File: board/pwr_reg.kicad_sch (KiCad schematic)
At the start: 52 parts, among them J2 9V-30VDC, Q1 IRF9540N, Q2 2N3906, Q3 IRF9540N, Q4 2N3906, SW1 On/Off, SW2 RESET, U1 LM350, U2 LM350, U3 LM350

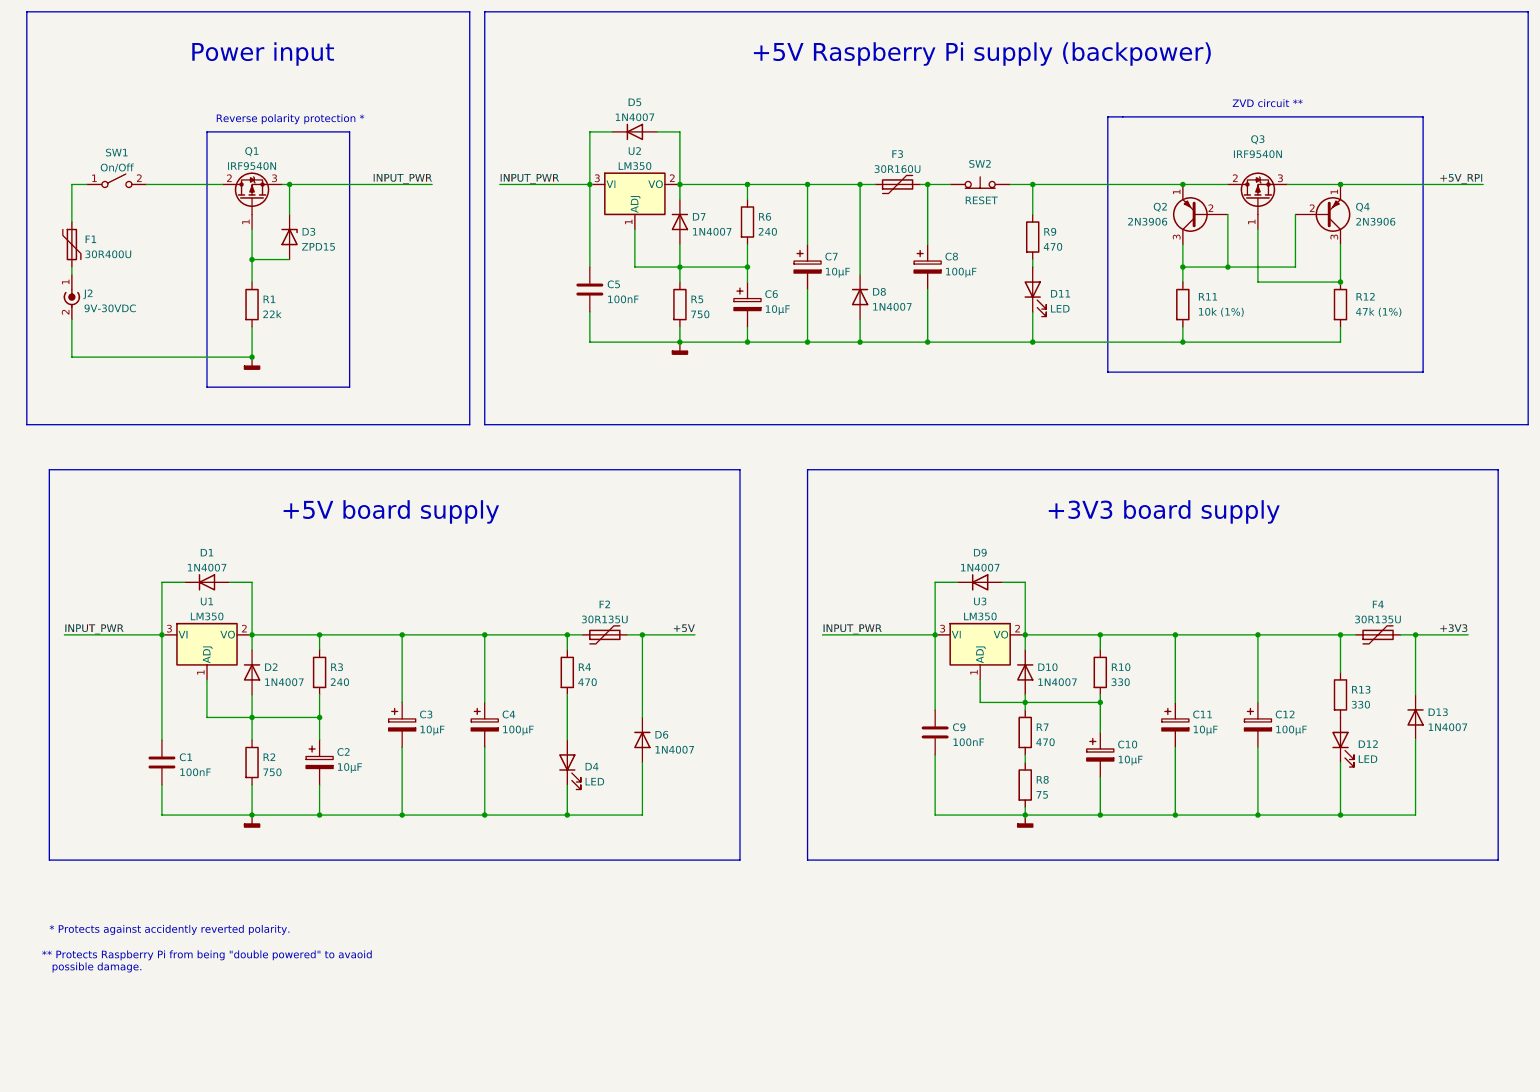
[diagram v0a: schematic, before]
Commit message: Make it a multiboard project.
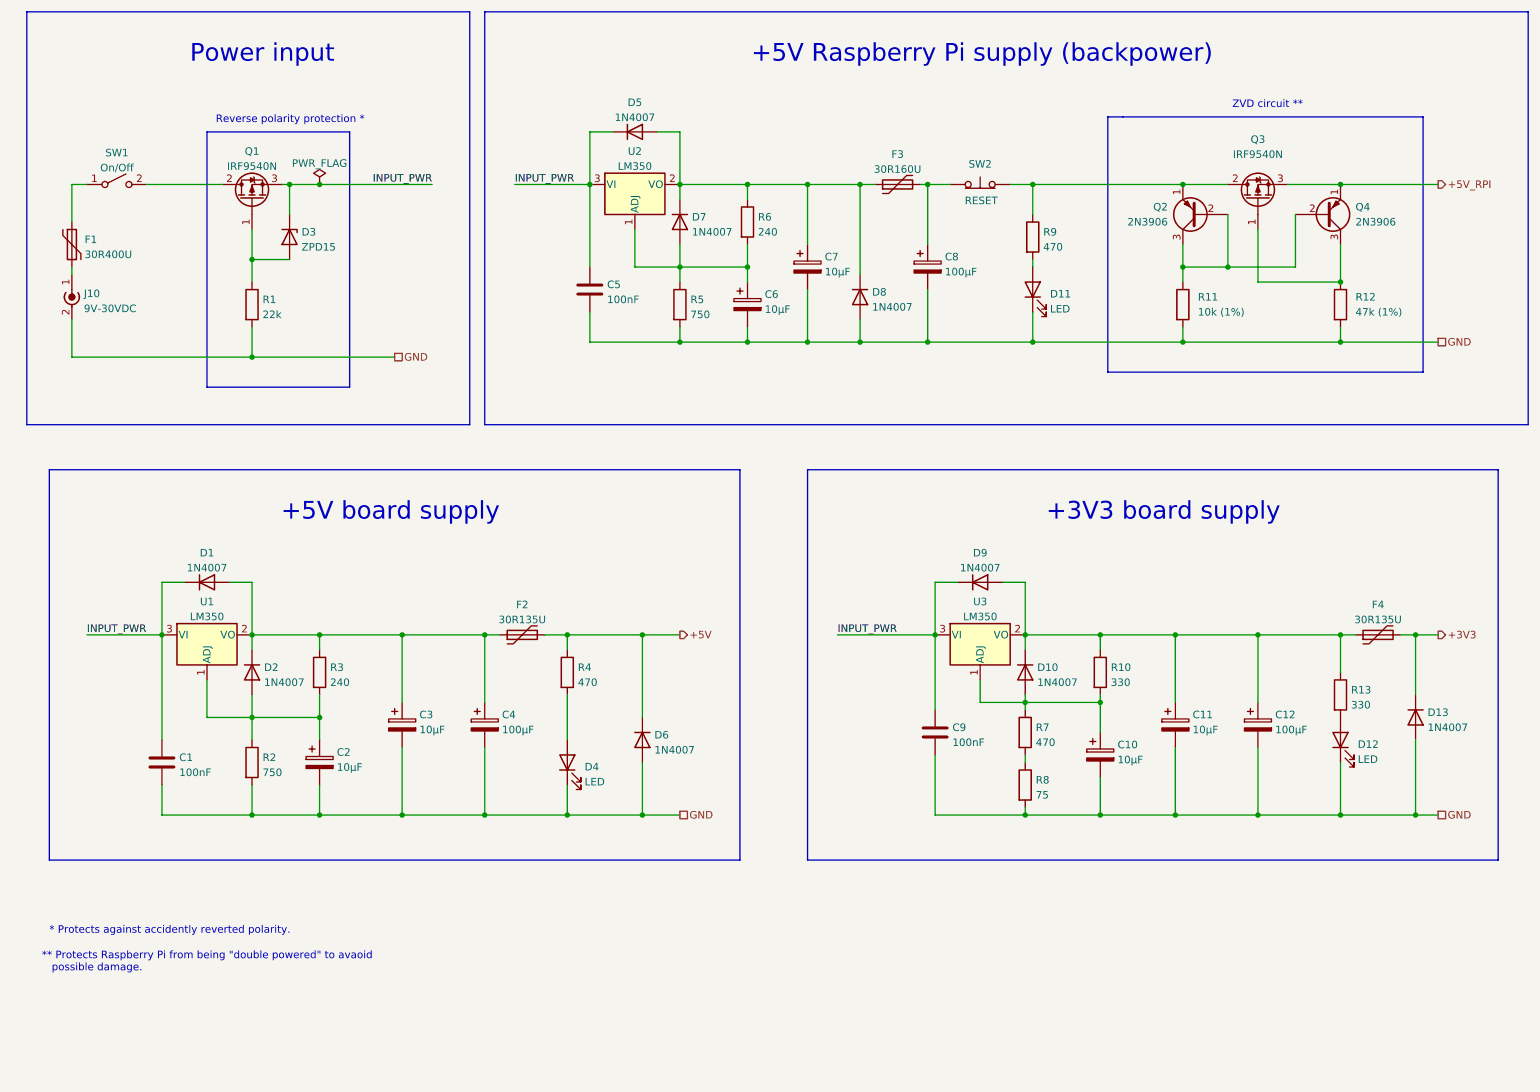
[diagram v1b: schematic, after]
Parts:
- renumbered J2 to J10
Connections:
- net +5V: now also R4.1
- net at C3.1, C4.1, D1.2 (A)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: no longer R4.1
- net GNDD renamed GND
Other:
- moved on the sheet: F2

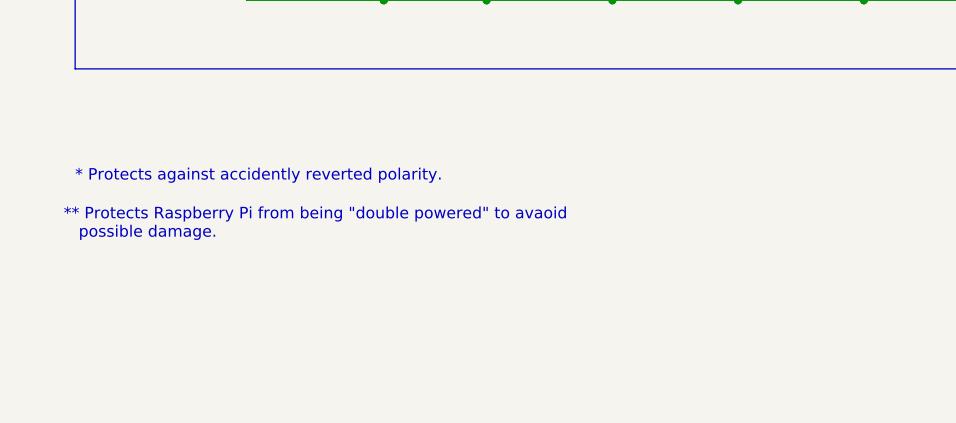
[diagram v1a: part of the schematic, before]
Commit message: Modularize board.
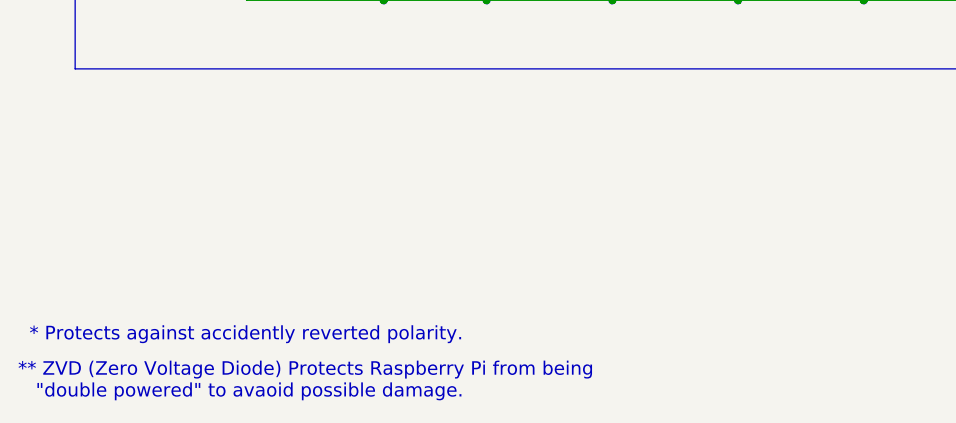
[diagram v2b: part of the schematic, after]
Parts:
- D1, D10, D13, D2, D5, D6, D7, D8, D9: footprint Diode_THT:D_DO-41_SOD81_P10.16mm_Horizontal -> Diode_THT:D_DO-41_SOD81_P5.08mm_Vertical_KathodeUp
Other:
- note added: "** ZVD (Zero Voltage Diode) Protects Raspberry Pi from being "double powered" to avaoid possible damage."
- note removed: "** Protects Raspberry Pi from being "double powered" to avaoid possible damage."
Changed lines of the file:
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@@
   (title_block
     (title "The Ulysses Board")
-    (date "2022-09-08")
+    (date "2022-09-15")
     (rev "1.3")
     (company "Dirk Gottschalk")
@@
     (effects (font (size 1.27 1.27)) (justify right bottom))
   )
-  (text "* Protects against accidently reverted polarity." (at 21.59 171.45 0)
-    (effects (font (size 1.27 1.27)) (justify left bottom))
+  (text "* Protects against accidently reverted polarity." (at 16.51 189.23 0)
+    (effects (font (size 1.5 1.5)) (justify left bottom))
   )
   (text "Reverse polarity protection *" (at 74.93 34.29 180)
@@
     (effects (font (size 3 3)) (justify right bottom))
   )
-  (text "** Protects Raspberry Pi from being \"double powered\" to avaoid\n   possible damage."
-    (at 20.32 177.8 0)
-    (effects (font (size 1.27 1.27)) (justify left bottom))
+  (text "** ZVD (Zero Voltage Diode) Protects Raspberry Pi from being\n   \"double powered\" to avaoid possible damage."
+    (at 15.24 195.58 0)
+    (effects (font (size 1.5 1.5)) (justify left bottom))
   )
   (text "+3V3 board supply" (at 229.87 101.6 180)
@@
     (property "Reference" "D9" (id 0) (at 179.07 106.7902 0))
     (property "Value" "1N4007" (id 1) (at 179.07 109.3271 0))
-    (property "Footprint" "Diode_THT:D_DO-41_SOD81_P10.16mm_Horizontal" (id 2) (at 179.07 116.205 0)
+    (property "Footprint" "Diode_THT:D_DO-41_SOD81_P5.08mm_Vertical_KathodeUp" (id 2) (at 179.07 116.205 0)
       (effects (font (size 1.27 1.27)) hide)
     )
@@
     (property "Reference" "D5" (id 0) (at 120.65 30.5902 0))
     (property "Value" "1N4007" (id 1) (at 120.65 33.1271 0))
-    (property "Footprint" "Diode_THT:D_DO-41_SOD81_P10.16mm_Horizontal" (id 2) (at 120.65 40.005 0)
+    (property "Footprint" "Diode_THT:D_DO-41_SOD81_P5.08mm_Vertical_KathodeUp" (id 2) (at 120.65 40.005 0)
       (effects (font (size 1.27 1.27)) hide)
     )
@@
       (effects (font (size 1.27 1.27)) (justify left))
     )
-    (property "Footprint" "Diode_THT:D_DO-41_SOD81_P10.16mm_Horizontal" (id 2) (at 182.245 127 0)
+    (property "Footprint" "Diode_THT:D_DO-41_SOD81_P5.08mm_Vertical_KathodeUp" (id 2) (at 182.245 127 0)
       (effects (font (size 1.27 1.27)) hide)
     )
@@
       (effects (font (size 1.27 1.27)) (justify left))
     )
-    (property "Footprint" "Diode_THT:D_DO-41_SOD81_P10.16mm_Horizontal" (id 2) (at 154.305 63.5 0)
+    (property "Footprint" "Diode_THT:D_DO-41_SOD81_P5.08mm_Vertical_KathodeUp" (id 2) (at 154.305 63.5 0)
       (effects (font (size 1.27 1.27)) hide)
     )
@@
       (effects (font (size 1.27 1.27)) (justify left))
     )
-    (property "Footprint" "Diode_THT:D_DO-41_SOD81_P10.16mm_Horizontal" (id 2) (at 123.825 50.8 0)
+    (property "Footprint" "Diode_THT:D_DO-41_SOD81_P5.08mm_Vertical_KathodeUp" (id 2) (at 123.825 50.8 0)
       (effects (font (size 1.27 1.27)) hide)
     )
@@
     (property "Reference" "D1" (id 0) (at 48.26 106.7902 0))
     (property "Value" "1N4007" (id 1) (at 48.26 109.3271 0))
-    (property "Footprint" "Diode_THT:D_DO-41_SOD81_P10.16mm_Horizontal" (id 2) (at 48.26 116.205 0)
+    (property "Footprint" "Diode_THT:D_DO-41_SOD81_P5.08mm_Vertical_KathodeUp" (id 2) (at 48.26 116.205 0)
       (effects (font (size 1.27 1.27)) hide)
     )
@@
       (effects (font (size 1.27 1.27)) (justify left))
     )
-    (property "Footprint" "Diode_THT:D_DO-41_SOD81_P10.16mm_Horizontal" (id 2) (at 117.475 138.43 0)
+    (property "Footprint" "Diode_THT:D_DO-41_SOD81_P5.08mm_Vertical_KathodeUp" (id 2) (at 117.475 138.43 0)
       (effects (font (size 1.27 1.27)) hide)
     )
@@
       (effects (font (size 1.27 1.27)) (justify left))
     )
-    (property "Footprint" "Diode_THT:D_DO-41_SOD81_P10.16mm_Horizontal" (id 2) (at 51.435 127 0)
+    (property "Footprint" "Diode_THT:D_DO-41_SOD81_P5.08mm_Vertical_KathodeUp" (id 2) (at 51.435 127 0)
       (effects (font (size 1.27 1.27)) hide)
     )
@@
       (effects (font (size 1.27 1.27)) (justify left))
     )
-    (property "Footprint" "Diode_THT:D_DO-41_SOD81_P10.16mm_Horizontal" (id 2) (at 248.285 134.62 0)
-      (effects (font (size 1.27 1.27)) hide)
-    )
+    (property "Footprint" "Diode_THT:D_DO-41_SOD81_P5.08mm_Vertical_KathodeUp" (id 2) (at 248.285 134.62 0)
+      (effects (font (size 1.27 1.27)) hide)
+    )
